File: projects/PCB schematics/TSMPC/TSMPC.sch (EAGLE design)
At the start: 23 parts

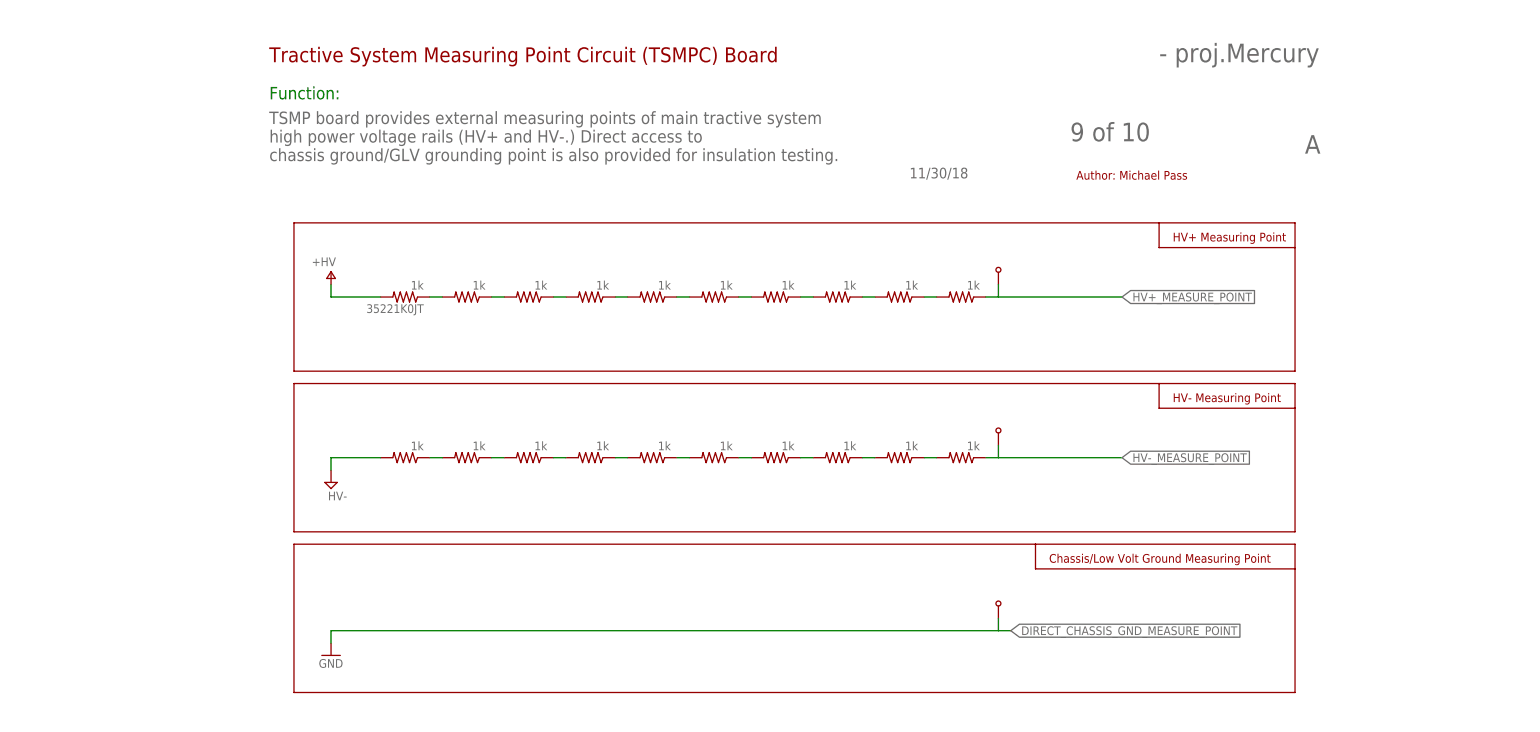
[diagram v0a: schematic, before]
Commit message: SC - Rev A; First PCB revision complete.
This marks the first draft of the SC board.
Parts have been laid out and initial routing completed through
extensive use of autorouter.
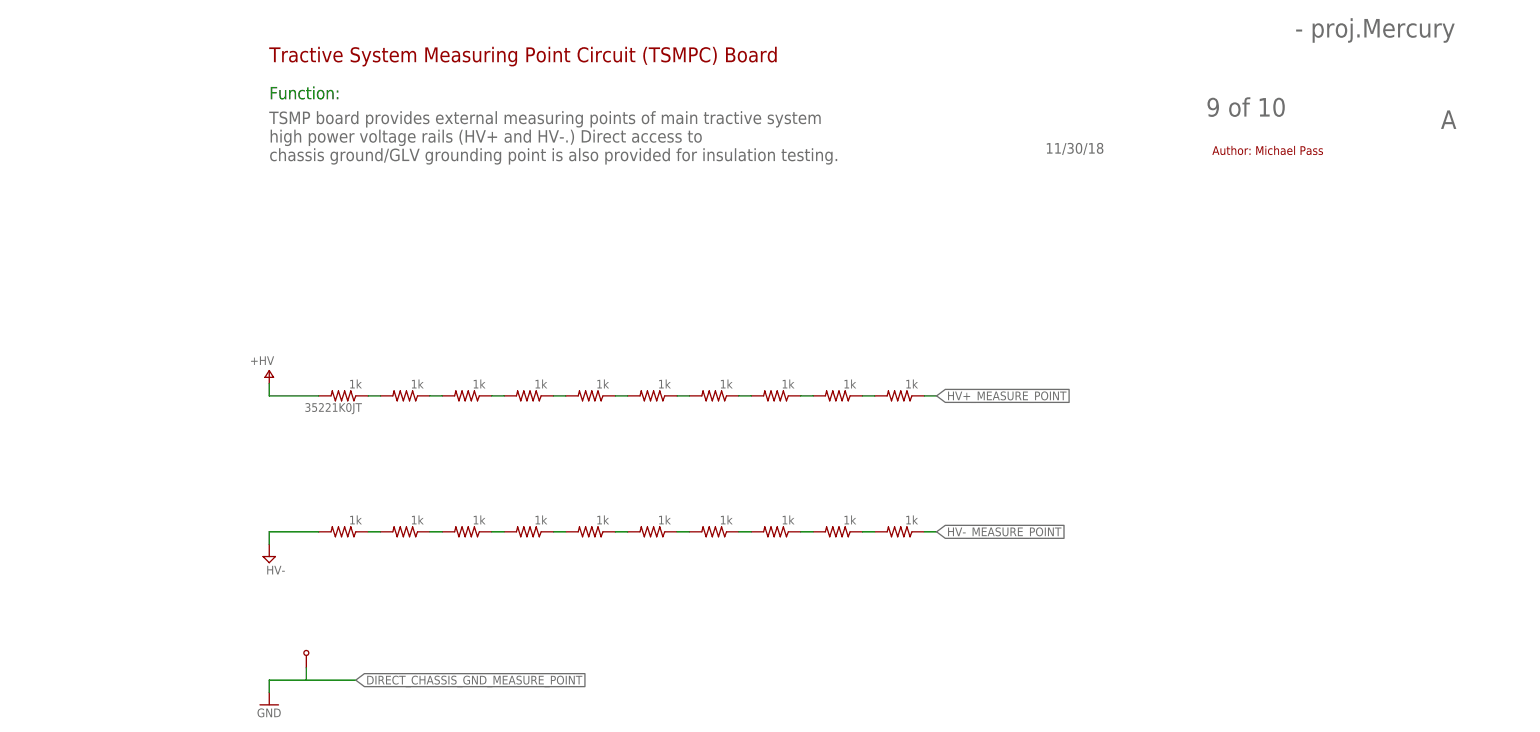
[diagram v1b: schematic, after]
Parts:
- removed U$1, U$4: BANANA-JACK, con-banana:BANANA-JACK
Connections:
- net HV+_MEASURE_POINT: no longer U$1.PIN
- net HV-_MEASURE_POINT: no longer U$4.PIN
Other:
- note removed: "Chassis/Low Volt Ground Measuring Point"
- note removed: "HV+ Measuring Point"
- note removed: "HV- Measuring Point"
- moved on the sheet: 35221K0JT

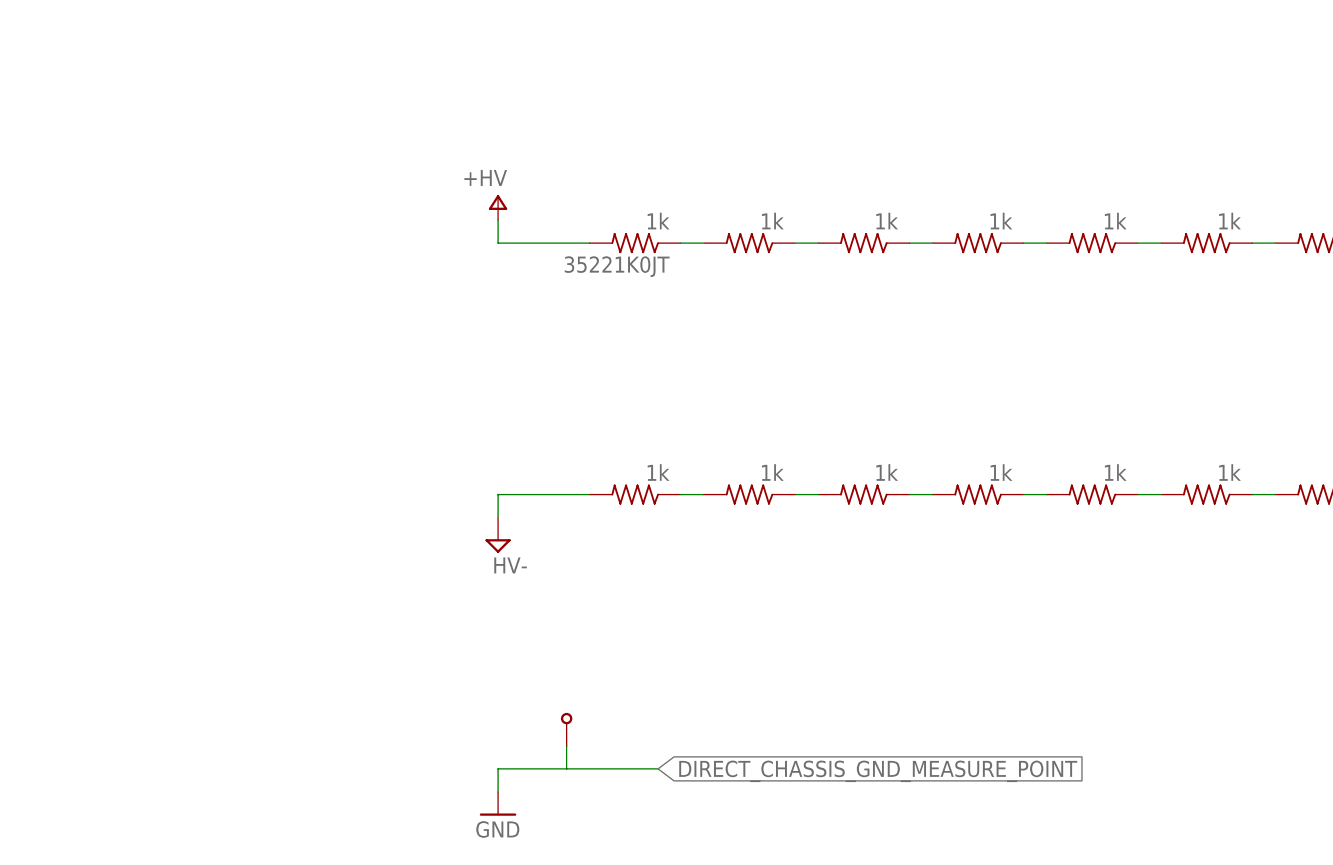
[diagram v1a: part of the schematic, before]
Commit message: TSMPC - Initial draft (WIP).
Non-working commit of TSMPC.
Done simply to show possible board layout.
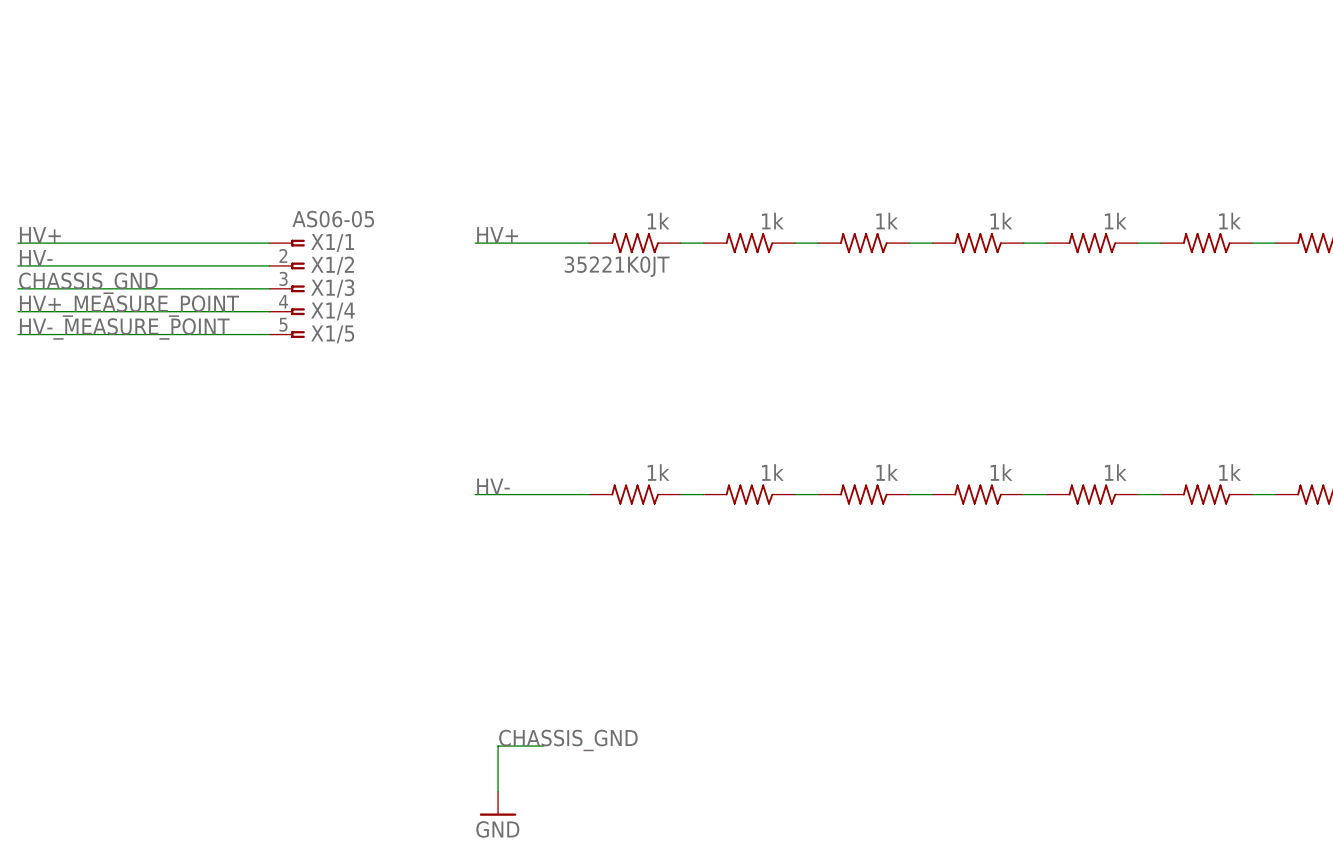
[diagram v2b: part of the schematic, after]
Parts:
- removed U$3: BANANA-JACK, con-banana:BANANA-JACK
- added X1: AS06-05, con-deutsch:AS06-05
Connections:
- removed net DIRECT_CHASSIS_GND_MEASURE_POINT: R21.2, U$3.PIN
- removed net V+: 35221K0JT.2
- new net CHASSIS_GND: X1/3.1
- new net HV+: 35221K0JT.2, X1/1.1
- new net HV-: R21.2, X1/2.1
- net HV+_MEASURE_POINT: now also X1/4.1
- net HV-_MEASURE_POINT: now also X1/5.1
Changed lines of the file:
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@@
 <setting verticaltext="up"/>
 </settings>
-<grid distance="0.1" unitdist="inch" unit="inch" style="lines" multiple="1" display="no" altdistance="0.01" altunitdist="inch" altunit="inch"/>
+<grid distance="0.1" unitdist="inch" unit="inch" style="lines" multiple="1" display="yes" altdistance="0.01" altunitdist="inch" altunit="inch"/>
 <layers>
 <layer number="1" name="Top" color="4" fill="1" visible="no" active="no"/>
@@
 <part name="FRAME2" library="frames" library_urn="urn:adsk.eagle:library:229" deviceset="FRAME_A_L" device=""/>
 <part name="35221K0JT" library="rcl" library_urn="urn:adsk.eagle:library:334" deviceset="R-US_" device="R0805" package3d_urn="urn:adsk.eagle:package:23553/2" value="1k"/>
-<part name="+5V2" library="supply1" library_urn="urn:adsk.eagle:library:371" deviceset="V+" device="" value="+HV"/>
 <part name="GND2" library="supply1" library_urn="urn:adsk.eagle:library:371" deviceset="GND" device=""/>
 <part name="R2" library="rcl" library_urn="urn:adsk.eagle:library:334" deviceset="R-US_" device="R0805" package3d_urn="urn:adsk.eagle:package:23553/2" value="1k"/>
@@
 <part name="R9" library="rcl" library_urn="urn:adsk.eagle:library:334" deviceset="R-US_" device="R0805" package3d_urn="urn:adsk.eagle:package:23553/2" value="1k"/>
 <part name="R10" library="rcl" library_urn="urn:adsk.eagle:library:334" deviceset="R-US_" device="R0805" package3d_urn="urn:adsk.eagle:package:23553/2" value="1k"/>
-<part name="U$3" library="con-banana" deviceset="BANANA-JACK" device=""/>
 <part name="R21" library="rcl" library_urn="urn:adsk.eagle:library:334" deviceset="R-US_" device="R0805" package3d_urn="urn:adsk.eagle:package:23553/2" value="1k"/>
 <part name="R22" library="rcl" library_urn="urn:adsk.eagle:library:334" deviceset="R-US_" device="R0805" package3d_urn="urn:adsk.eagle:package:23553/2" value="1k"/>
@@
 <part name="R29" library="rcl" library_urn="urn:adsk.eagle:library:334" deviceset="R-US_" device="R0805" package3d_urn="urn:adsk.eagle:package:23553/2" value="1k"/>
 <part name="R30" library="rcl" library_urn="urn:adsk.eagle:library:334" deviceset="R-US_" device="R0805" package3d_urn="urn:adsk.eagle:package:23553/2" value="1k"/>
-<part name="SUPPLY1" library="supply2" library_urn="urn:adsk.eagle:library:372" deviceset="GND" device="" value="HV-"/>
+<part name="X1" library="con-deutsch" library_urn="urn:adsk.eagle:library:139" deviceset="AS06-05" device="" package3d_urn="urn:adsk.eagle:package:6519/1"/>
 </parts>
 <sheets>
@@
 <attribute name="VALUE" x="29.21" y="74.422" size="1.778" layer="96" rot="R180"/>
 </instance>
-<instance part="+5V2" gate="1" x="10.16" y="76.2" smashed="yes">
-<attribute name="VALUE" x="11.176" y="79.248" size="1.778" layer="96" rot="R180"/>
-</instance>
 <instance part="GND2" gate="1" x="10.16" y="7.62" smashed="yes">
 <attribute name="VALUE" x="7.62" y="5.08" size="1.778" layer="96"/>
@@
 <attribute name="VALUE" x="143.51" y="74.422" size="1.778" layer="96" rot="R180"/>
 </instance>
-<instance part="U$3" gate="G$1" x="17.78" y="17.78" smashed="yes" rot="R270"/>
 <instance part="R21" gate="G$1" x="25.4" y="43.18" smashed="yes" rot="R180">
 <attribute name="VALUE" x="29.21" y="46.482" size="1.778" layer="96" rot="R180"/>
@@
 <attribute name="VALUE" x="143.51" y="46.482" size="1.778" layer="96" rot="R180"/>
 </instance>
-<instance part="SUPPLY1" gate="GND" x="10.16" y="38.1" smashed="yes">
-<attribute name="VALUE" x="9.525" y="34.417" size="1.778" layer="96"/>
+<instance part="X1" gate="/1" x="-12.7" y="71.12" smashed="yes">
+<attribute name="NAME" x="-10.668" y="70.358" size="1.778" layer="95"/>
+<attribute name="VALUE" x="-12.7" y="72.898" size="1.778" layer="96"/>
+</instance>
+<instance part="X1" gate="/2" x="-12.7" y="68.58" smashed="yes">
+<attribute name="NAME" x="-10.668" y="67.818" size="1.778" layer="95"/>
+</instance>
+<instance part="X1" gate="/3" x="-12.7" y="66.04" smashed="yes">
+<attribute name="NAME" x="-10.668" y="65.278" size="1.778" layer="95"/>
+</instance>
+<instance part="X1" gate="/4" x="-12.7" y="63.5" smashed="yes">
+<attribute name="NAME" x="-10.668" y="62.738" size="1.778" layer="95"/>
+</instance>
+<instance part="X1" gate="/5" x="-12.7" y="60.96" smashed="yes">
+<attribute name="NAME" x="-10.668" y="60.198" size="1.778" layer="95"/>
 </instance>
 </instances>
@@
 </busses>
 <nets>
-<net name="V+" class="0">
-<segment>
-<pinref part="+5V2" gate="1" pin="V+"/>
-<wire x1="10.16" y1="73.66" x2="10.16" y2="71.12" width="0.1524" layer="91"/>
-<pinref part="35221K0JT" gate="G$1" pin="2"/>
-<wire x1="10.16" y1="71.12" x2="20.32" y2="71.12" width="0.1524" layer="91"/>
-</segment>
-</net>
 <net name="N$1" class="0">
 <segment>
@@
 <label x="147.32" y="71.12" size="1.778" layer="95" xref="yes"/>
 </segment>
-</net>
-<net name="DIRECT_CHASSIS_GND_MEASURE_POINT" class="0">
-<segment>
-<pinref part="GND2" gate="1" pin="GND"/>
-<wire x1="10.16" y1="10.16" x2="10.16" y2="12.7" width="0.1524" layer="91"/>
-<pinref part="U$3" gate="G$1" pin="PIN"/>
-<wire x1="10.16" y1="12.7" x2="17.78" y2="12.7" width="0.1524" layer="91"/>
-<wire x1="17.78" y1="12.7" x2="17.78" y2="15.24" width="0.1524" layer="91"/>
-<wire x1="17.78" y1="12.7" x2="27.94" y2="12.7" width="0.1524" layer="91"/>
-<label x="27.94" y="12.7" size="1.778" layer="95" xref="yes"/>
-</segment>
-<segment>
-<pinref part="R21" gate="G$1" pin="2"/>
-<wire x1="10.16" y1="43.18" x2="20.32" y2="43.18" width="0.1524" layer="91"/>
-<pinref part="SUPPLY1" gate="GND" pin="GND"/>
-<wire x1="10.16" y1="43.18" x2="10.16" y2="40.64" width="0.1524" layer="91"/>
+<segment>
+<pinref part="X1" gate="/4" pin="1"/>
+<label x="-43.18" y="63.5" size="1.778" layer="255"/>
+<wire x1="-15.24" y1="63.5" x2="-43.18" y2="63.5" width="0.1524" layer="91"/>
 </segment>
 </net>
@@
 <label x="147.32" y="43.18" size="1.778" layer="95" xref="yes"/>
 </segment>
-</net>
+<segment>
+<pinref part="X1" gate="/5" pin="1"/>
+<wire x1="-15.24" y1="60.96" x2="-43.18" y2="60.96" width="0.1524" layer="91"/>
+<label x="-43.18" y="60.96" size="1.778" layer="255"/>
+</segment>
+</net>
+<net name="HV+" class="0">
+<segment>
+<pinref part="X1" gate="/1" pin="1"/>
+<wire x1="-15.24" y1="71.12" x2="-43.18" y2="71.12" width="0.1524" layer="91"/>
+<label x="-43.18" y="71.12" size="1.778" layer="95"/>
+</segment>
+<segment>
+<pinref part="35221K0JT" gate="G$1" pin="2"/>
+<wire x1="20.32" y1="71.12" x2="7.62" y2="71.12" width="0.1524" layer="91"/>
+<label x="7.62" y="71.12" size="1.778" layer="255"/>
+</segment>
+</net>
+<net name="HV-" class="0">
+<segment>
+<wire x1="-15.24" y1="68.58" x2="-43.18" y2="68.58" width="0.1524" layer="91"/>
+<pinref part="X1" gate="/2" pin="1"/>
+<label x="-43.18" y="68.58" size="1.778" layer="95"/>
+</segment>
+<segment>
+<pinref part="R21" gate="G$1" pin="2"/>
+<wire x1="20.32" y1="43.18" x2="7.62" y2="43.18" width="0.1524" layer="91"/>
+<label x="7.62" y="43.18" size="1.778" layer="255"/>
+</segment>
+</net>
+<net name="CHASSIS_GND" class="0">
+<segment>
+<pinref part="GND2" gate="1" pin="GND"/>
+<wire x1="10.16" y1="10.16" x2="10.16" y2="15.24" width="0.1524" layer="91"/>
+<wire x1="10.16" y1="15.24" x2="15.24" y2="15.24" width="0.1524" layer="91"/>
+<label x="10.16" y="15.24" size="1.778" layer="255"/>
+</segment>
+<segment>
+<wire x1="-15.24" y1="66.04" x2="-43.18" y2="66.04" width="0.1524" layer="91"/>
+<pinref part="X1" gate="/3" pin="1"/>
+<label x="-43.18" y="66.04" size="1.778" layer="95"/>
+</segment>
+</net>

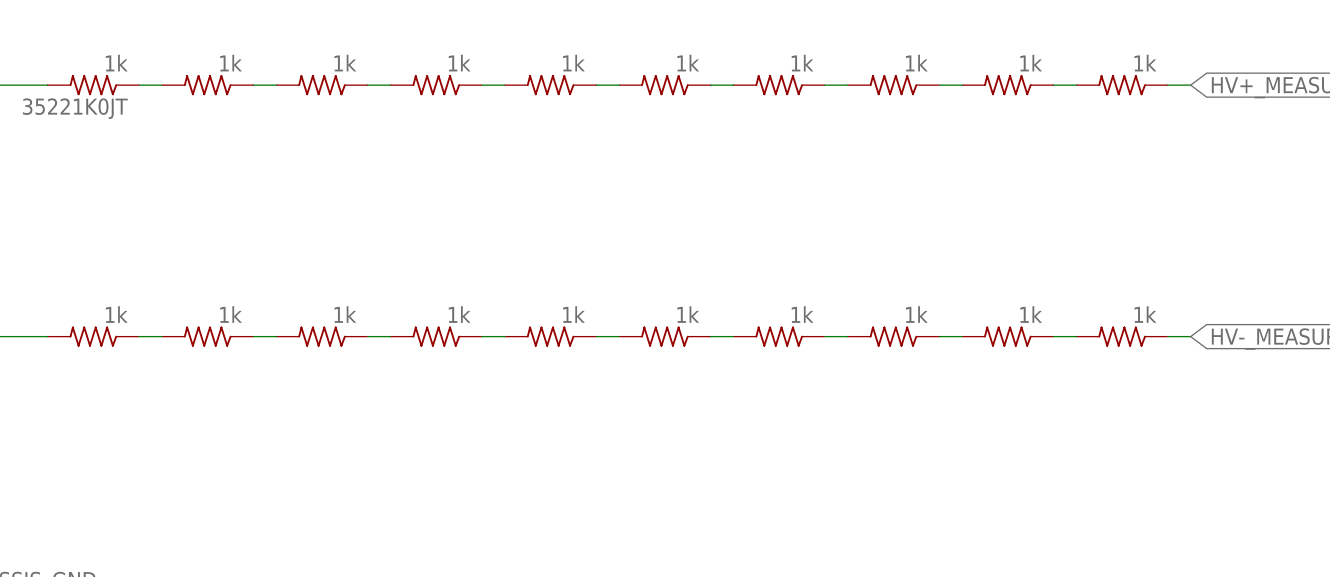
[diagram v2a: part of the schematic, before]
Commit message: BSPD - Schematic revision/component revision.
During ESF, schematics chosen used European part libraries.
These were updated to US symbols, with appropriate final parts sourced
to allow builds of both SOP8 and DIL-8 packages.
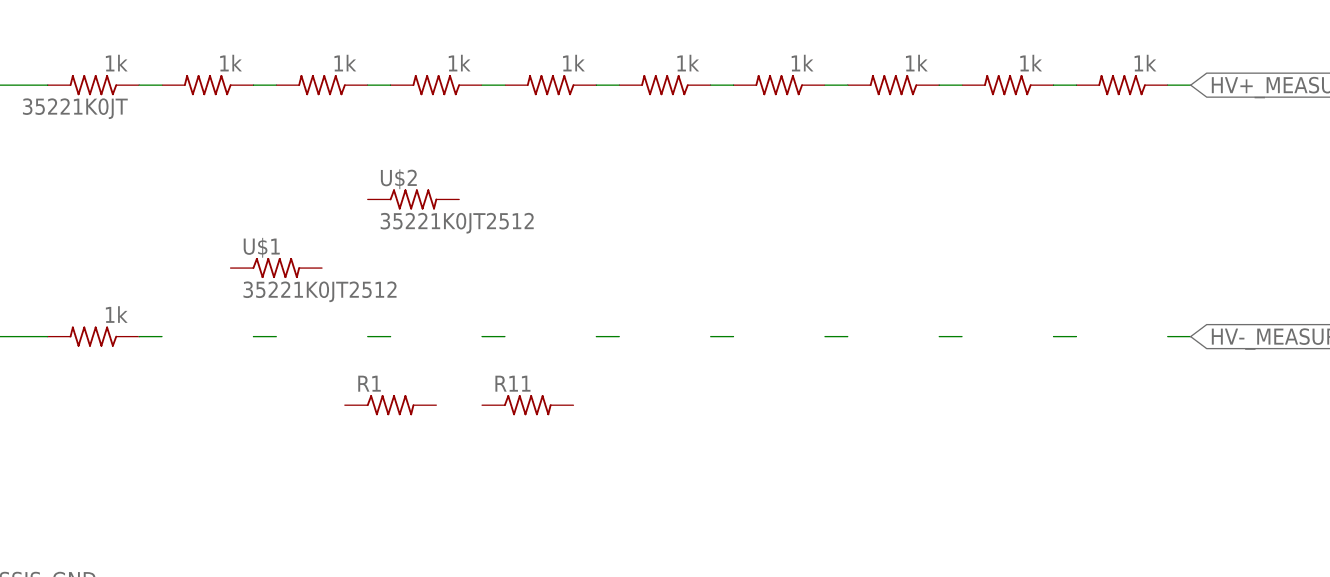
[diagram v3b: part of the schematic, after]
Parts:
- removed R22, R23, R24, R25, R26, R27, R28, R29, R30: 1k, rcl:R-US_R0805
- added R1, R11: (no value), rcl:R-US_R0805
- added U$1, U$2: 35221K0JT2512, IowaFormula:35221K0JT2512
- R21: device rcl:R-US_R0805 -> rcl:R-US_R2512
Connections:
- removed net N$22: R22.1, R23.2
- removed net N$23: R23.1, R24.2
- removed net N$24: R24.1, R25.2
- removed net N$25: R25.1, R26.2
- removed net N$26: R26.1, R27.2
- removed net N$27: R27.1, R28.2
- removed net N$28: R28.1, R29.2
- removed net N$29: R29.1, R30.2
- net HV-_MEASURE_POINT: no longer R30.1
- net N$21: no longer R22.2
